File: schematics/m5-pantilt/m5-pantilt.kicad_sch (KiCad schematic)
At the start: 33 parts, among them J1 Conn_02x15_Odd_Even, J2 Conn_02x15_Odd_Even, J3 Conn_01x03, J5 BAT, J6 Conn_01x04, J7 5V_POWER, J8 Conn_01x03, Q1 IRLML6402, Q2 BC857, SW1 SW_SPDT, U1 MAX3485

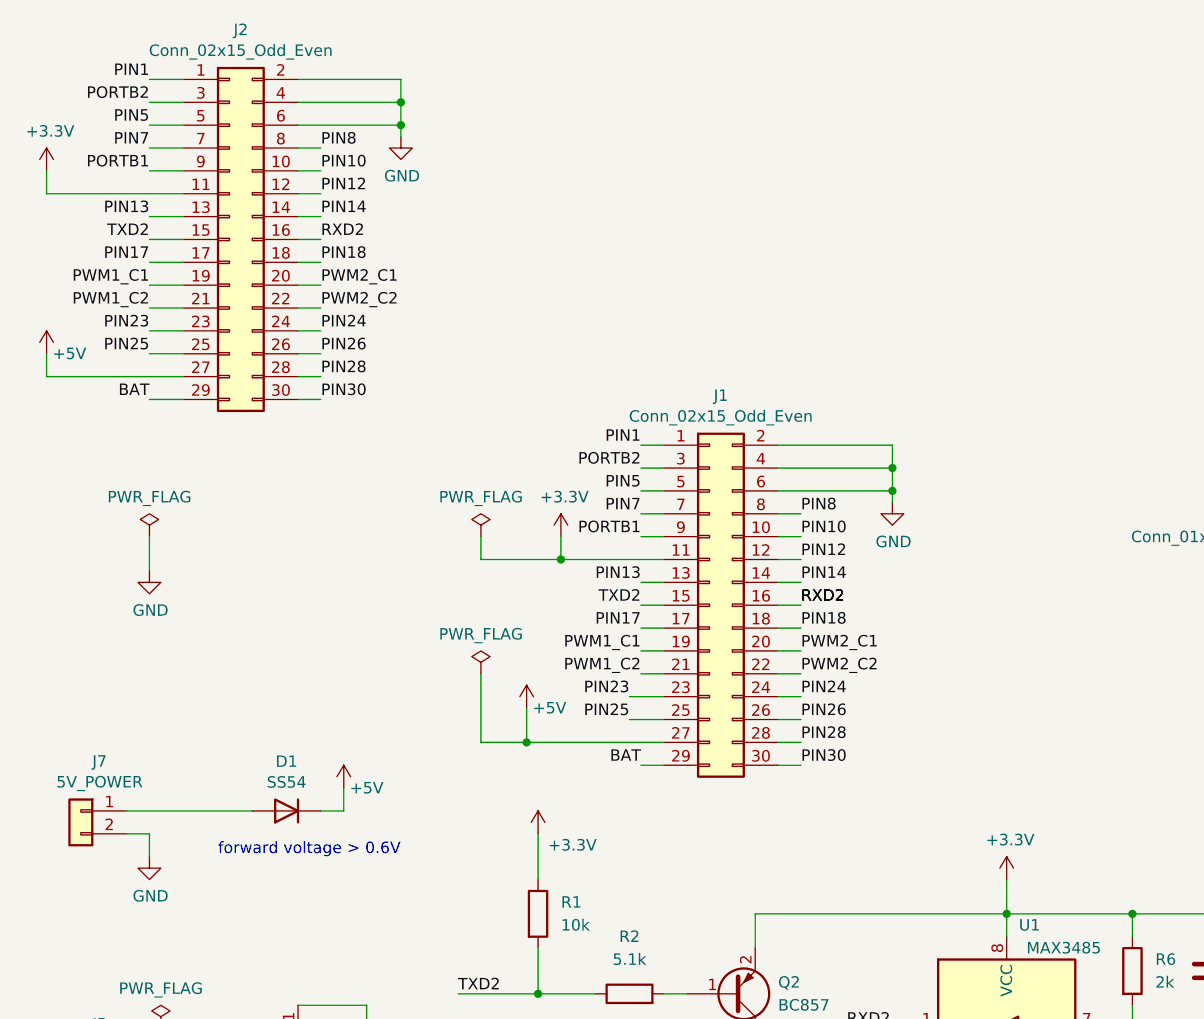
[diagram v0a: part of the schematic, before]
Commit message: 部品、いくつかのfootprint変更
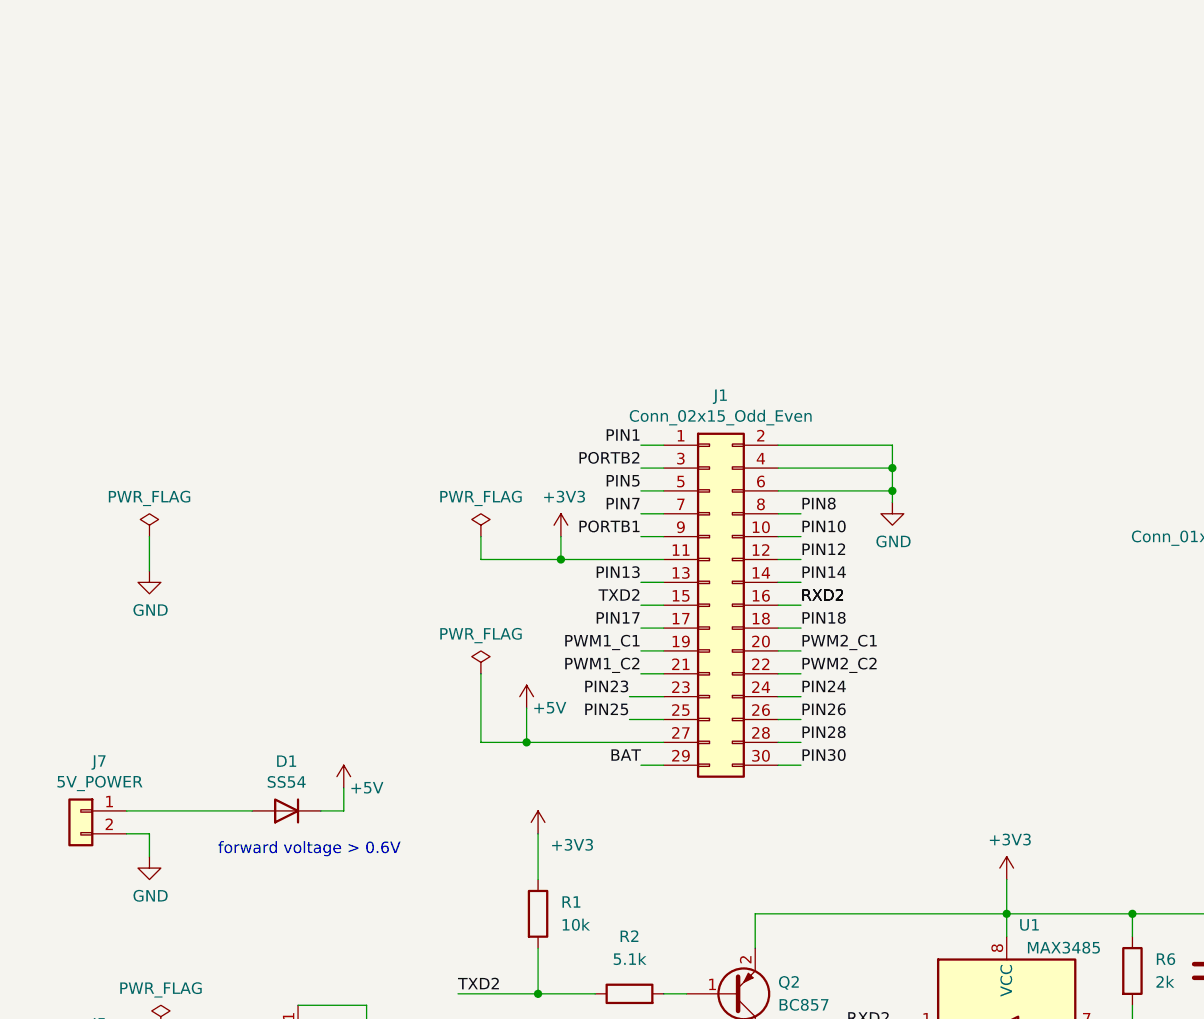
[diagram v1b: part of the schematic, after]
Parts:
- removed J2: Conn_02x15_Odd_Even, Connector_PinSocket_2.54mm:PinSocket_2x15_P2.54mm_Vertical_SMD, symbol Connector_Generic:Conn_02x15_Odd_Even
